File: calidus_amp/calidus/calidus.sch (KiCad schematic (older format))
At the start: 15 parts, among them J1 power, J10 led_overload, J11 led_power, J2 input, J3 prevs, J4 icsp, J5 service, J6 sense_bus, J7 left_out, J8 right_out, J9 mute_key

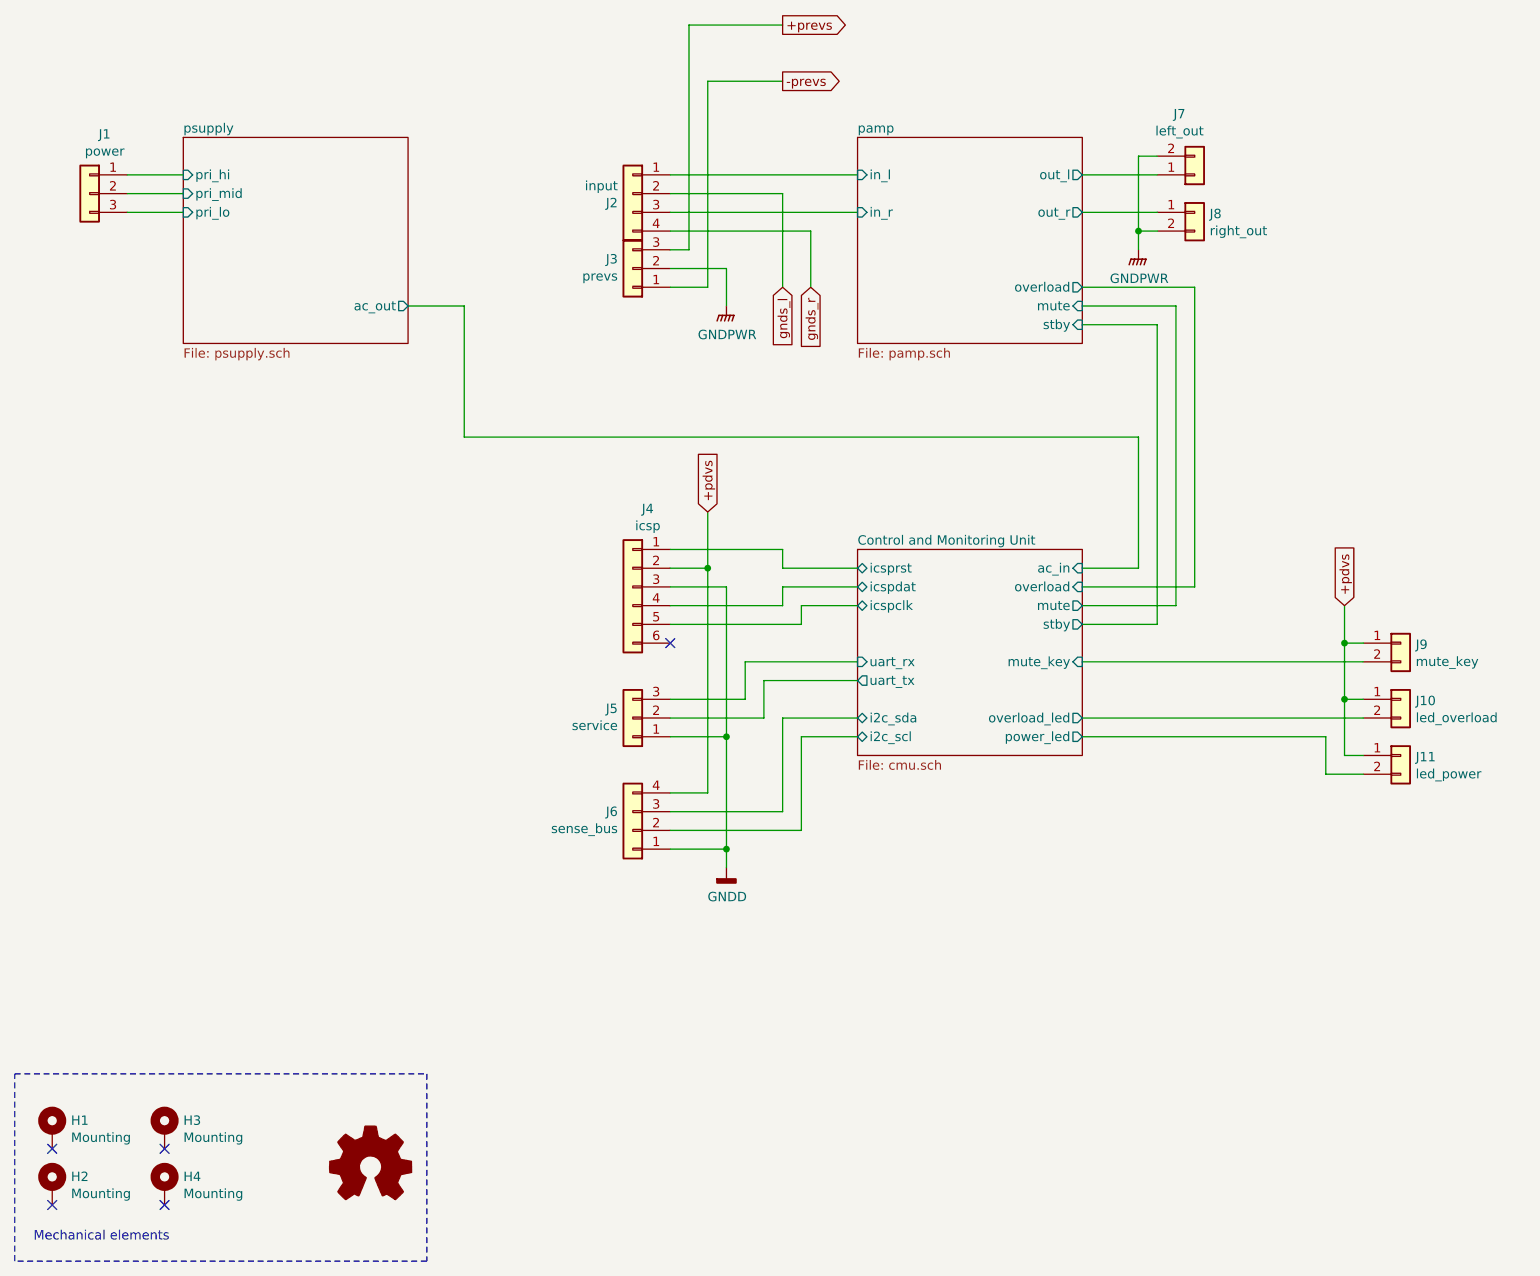
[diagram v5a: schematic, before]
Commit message: WIP: Component placement on PCB
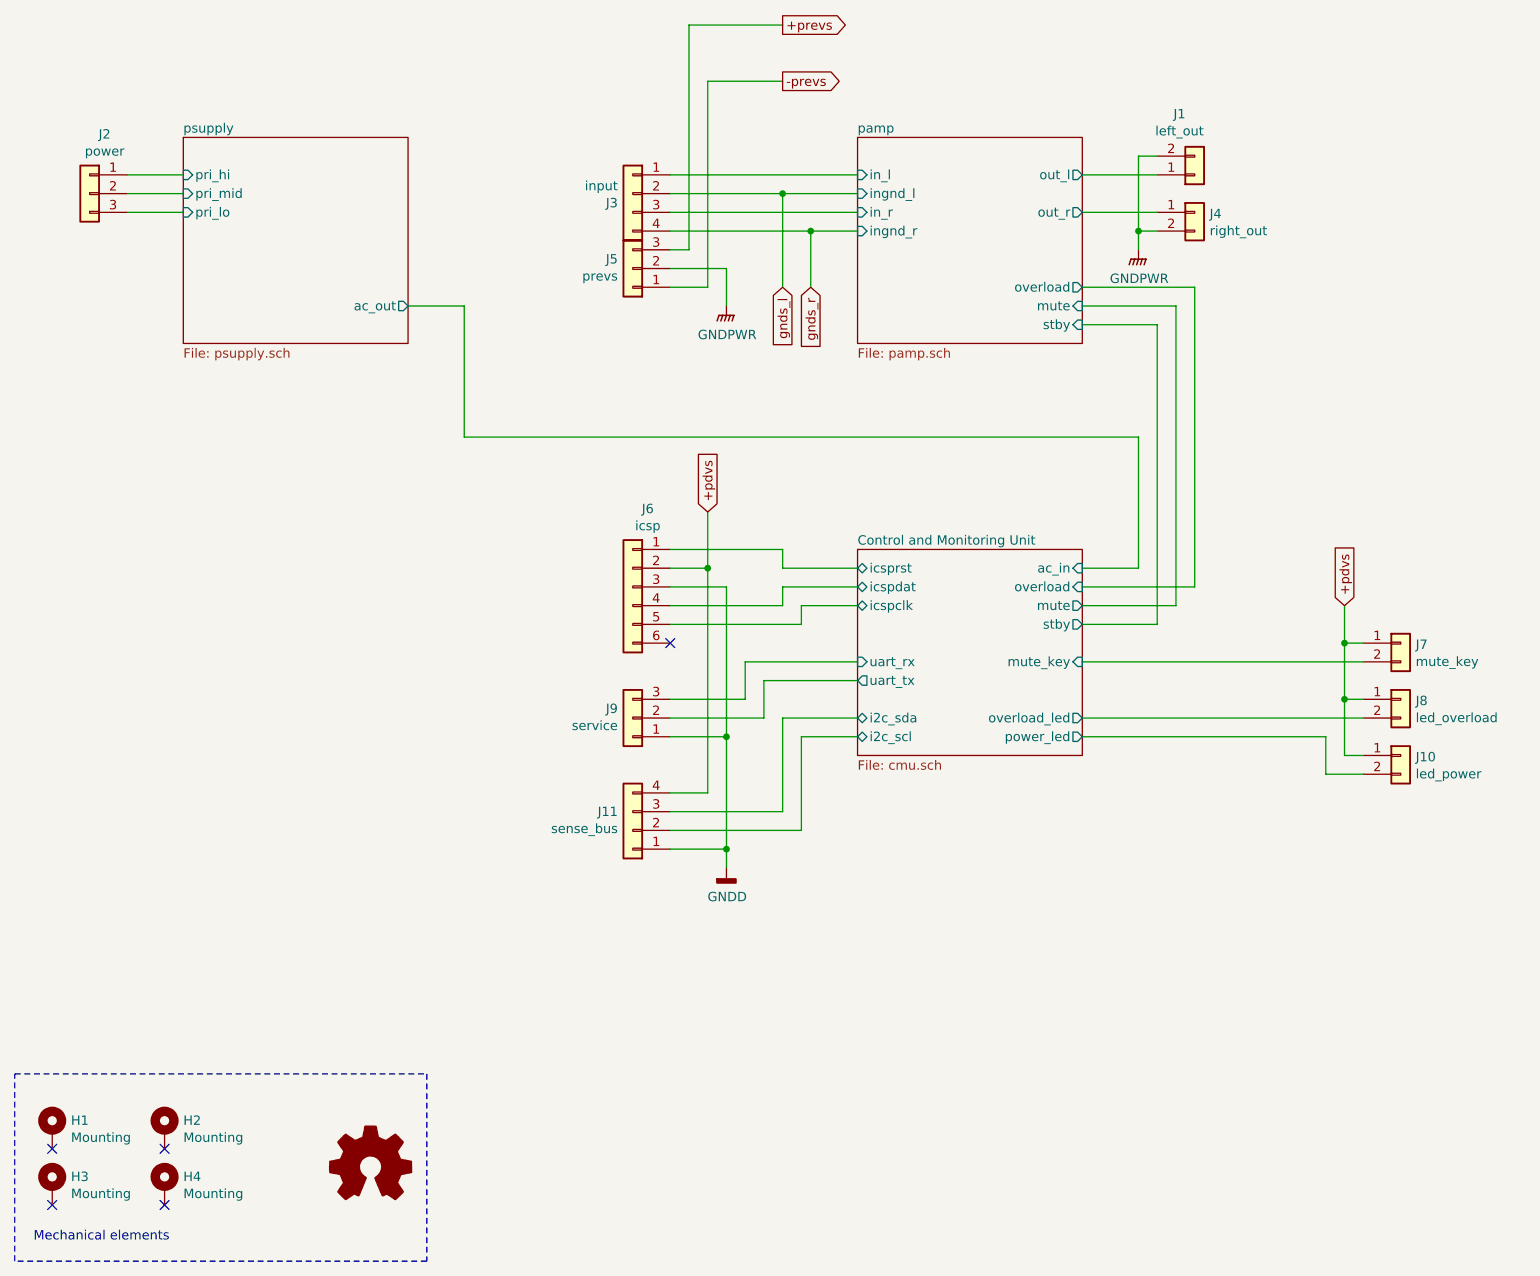
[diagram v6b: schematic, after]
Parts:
- renumbered H3 to H2, H2 to H3, J7 to J1, J11 to J10, J6 to J11, J1 to J2, J2 to J3, J8 to J4, J3 to J5, J4 to J6, J9 to J7, J10 to J8, J5 to J9
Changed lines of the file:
@@
 F7 "out_r" O R 6700 2000 50
 F8 "stby" I R 6700 2600 50
+F9 "ingnd_l" I L 5500 1900 50
+F10 "ingnd_r" I L 5500 2100 50
 $EndSheet
 $Comp
-L Connector_Generic:Conn_01x03 J1
+L Connector_Generic:Conn_01x03 J2
 U 1 1 5C47FAB8
 P 1400 1900
-F 0 "J1" H 1320 2217 50  0000 C CNN
+F 0 "J2" H 1320 2217 50  0000 C CNN
 F 1 "power" H 1320 2126 50  0000 C CNN
 F 2 "Connector_Phoenix_MC:PhoenixContact_MCV_1,5_3-G-3.5_1x03_P3.50mm_Vertical" H 1400 1900 50  0001 C CNN
@@
 	5100 1900 4500 1900
 $Comp
-L Connector_Generic:Conn_01x02 J7
+L Connector_Generic:Conn_01x02 J1
 U 1 1 5C47FBF8
 P 7300 1800
-F 0 "J7" H 7219 1475 50  0000 C CNN
+F 0 "J1" H 7219 1475 50  0000 C CNN
 F 1 "left_out" H 7219 1566 50  0000 C CNN
 F 2 "Connector_Phoenix_MC:PhoenixContact_MCV_1,5_2-G-3.5_1x02_P3.50mm_Vertical" H 7300 1800 50  0001 C CNN
@@
 $EndComp
 $Comp
-L Connector_Generic:Conn_01x02 J8
+L Connector_Generic:Conn_01x02 J4
 U 1 1 5C47FC30
 P 7300 2000
-F 0 "J8" H 7380 1992 50  0000 L CNN
+F 0 "J4" H 7380 1992 50  0000 L CNN
 F 1 "right_out" H 7380 1901 50  0000 L CNN
 F 2 "Connector_Phoenix_MC:PhoenixContact_MCV_1,5_2-G-3.5_1x02_P3.50mm_Vertical" H 7300 2000 50  0001 C CNN
@@
 	7000 2100 7100 2100
 $Comp
-L power:GNDPWR #PWR04
+L power:GNDPWR #PWR01
 U 1 1 5C47FEE1
 P 7000 2200
-F 0 "#PWR04" H 7000 2000 50  0001 C CNN
+F 0 "#PWR01" H 7000 2000 50  0001 C CNN
 F 1 "GNDPWR" H 7004 2046 50  0000 C CNN
 F 2 "" H 7000 2150 50  0001 C CNN
@@
 +pdvs
 $Comp
-L Connector_Generic:Conn_01x02 J10
+L Connector_Generic:Conn_01x02 J8
 U 1 1 5C4DAFE8
 P 8400 4600
-F 0 "J10" H 8480 4592 50  0000 L CNN
+F 0 "J8" H 8480 4592 50  0000 L CNN
 F 1 "led_overload" H 8480 4501 50  0000 L CNN
 F 2 "Connector_PinHeader_2.54mm:PinHeader_1x02_P2.54mm_Vertical" H 8400 4600 50  0001 C CNN
@@
 $EndComp
 $Comp
-L Connector_Generic:Conn_01x02 J11
+L Connector_Generic:Conn_01x02 J10
 U 1 1 5C4DB050
 P 8400 4900
-F 0 "J11" H 8480 4892 50  0000 L CNN
+F 0 "J10" H 8480 4892 50  0000 L CNN
 F 1 "led_power" H 8480 4801 50  0000 L CNN
 F 2 "Connector_PinHeader_2.54mm:PinHeader_1x02_P2.54mm_Vertical" H 8400 4900 50  0001 C CNN
@@
 Connection ~ 8100 4600
 $Comp
-L Connector_Generic:Conn_01x02 J9
+L Connector_Generic:Conn_01x02 J7
 U 1 1 5C4E1437
 P 8400 4300
-F 0 "J9" H 8480 4292 50  0000 L CNN
+F 0 "J7" H 8480 4292 50  0000 L CNN
 F 1 "mute_key" H 8480 4201 50  0000 L CNN
 F 2 "Connector_PinHeader_2.54mm:PinHeader_1x02_P2.54mm_Vertical" H 8400 4300 50  0001 C CNN
@@
 	7000 3900 6700 3900
 $Comp
-L Connector_Generic:Conn_01x06 J4
+L Connector_Generic:Conn_01x06 J6
 U 1 1 5C4F09AA
 P 4300 4000
-F 0 "J4" H 4220 4417 50  0000 C CNN
+F 0 "J6" H 4220 4417 50  0000 C CNN
 F 1 "icsp" H 4220 4326 50  0000 C CNN
 F 2 "Connector_PinHeader_2.54mm:PinHeader_1x06_P2.54mm_Vertical" H 4300 4000 50  0001 C CNN
@@
 P 4800 5500
 AR Path="/5C43C4AB/5C504FC8" Ref="#PWR?"  Part="1"
-AR Path="/5C504FC8" Ref="#PWR02"  Part="1"
-F 0 "#PWR02" H 4800 5250 50  0001 C CNN
+AR Path="/5C504FC8" Ref="#PWR03"  Part="1"
+F 0 "#PWR03" H 4800 5250 50  0001 C CNN
 F 1 "GNDD" H 4804 5345 50  0000 C CNN
 F 2 "" H 4800 5500 50  0001 C CNN
@@
 	4500 4200 5200 4200
 $Comp
-L Connector_Generic:Conn_01x03 J5
+L Connector_Generic:Conn_01x03 J9
 U 1 1 5C51607F
 P 4300 4700
-F 0 "J5" H 4380 4650 50  0000 L CNN
+F 0 "J9" H 4380 4650 50  0000 L CNN
 F 1 "service" H 4380 4741 50  0000 L CNN
 F 2 "Connector_PinHeader_2.54mm:PinHeader_1x03_P2.54mm_Vertical" H 4300 4700 50  0001 C CNN
@@
 	4800 4000 4500 4000
 $Comp
-L Connector_Generic:Conn_01x04 J6
+L Connector_Generic:Conn_01x04 J11
 U 1 1 5C5CE216
 P 4300 5300
-F 0 "J6" H 4380 5200 50  0000 L CNN
+F 0 "J11" H 4380 5200 50  0000 L CNN
 F 1 "sense_bus" H 4380 5291 50  0000 L CNN
 F 2 "Connector_PinHeader_2.54mm:PinHeader_1x04_P2.54mm_Vertical" H 4300 5300 50  0001 C CNN
@@
 NoConn ~ 1200 7000
 $Comp
-L Mechanical:MountingHole_Pad H2
+L Mechanical:MountingHole_Pad H3
 U 1 1 5C581F06
 P 1200 7200
-F 0 "H2" H 1300 7251 50  0000 L CNN
+F 0 "H3" H 1300 7251 50  0000 L CNN
 F 1 "Mounting" H 1300 7160 50  0000 L CNN
 F 2 "MountingHole:MountingHole_3.2mm_M3_Pad" H 1200 7200 50  0001 C CNN
@@
 NoConn ~ 1200 7300
 $Comp
-L Mechanical:MountingHole_Pad H3
+L Mechanical:MountingHole_Pad H2
 U 1 1 5C5841CE
 P 1800 6900
-F 0 "H3" H 1900 6951 50  0000 L CNN
+F 0 "H2" H 1900 6951 50  0000 L CNN
 F 1 "Mounting" H 1900 6860 50  0000 L CNN
 F 2 "MountingHole:MountingHole_3.2mm_M3_Pad" H 1800 6900 50  0001 C CNN
@@
 Mechanical elements
 $Comp
-L power:GNDPWR #PWR01
+L power:GNDPWR #PWR02
 U 1 1 5C50E81E
 P 4800 2500
-F 0 "#PWR01" H 4800 2300 50  0001 C CNN
+F 0 "#PWR02" H 4800 2300 50  0001 C CNN
 F 1 "GNDPWR" H 4804 2346 50  0000 C CNN
 F 2 "" H 4800 2450 50  0001 C CNN
@@
 	4600 1000 5100 1000
 $Comp
-L Connector_Generic:Conn_01x04 J2
+L Connector_Generic:Conn_01x04 J3
 U 1 1 5C540E50
 P 4300 1900
-F 0 "J2" H 4380 1850 50  0000 L CNN
+F 0 "J3" H 4380 1850 50  0000 L CNN
 F 1 "input" H 4380 1941 50  0000 L CNN
 F 2 "Connector_Phoenix_MC:PhoenixContact_MCV_1,5_3-G-3.5_1x03_P3.50mm_Vertical" H 4300 1900 50  0001 C CNN
@@
 $EndComp
 $Comp
-L Connector_Generic:Conn_01x03 J3
+L Connector_Generic:Conn_01x03 J5
 U 1 1 5C540ED0
 P 4300 2300
-F 0 "J3" H 4380 2250 50  0000 L CNN
+F 0 "J5" H 4380 2250 50  0000 L CNN
 F 1 "prevs" H 4380 2341 50  0000 L CNN
 F 2 "Connector_Phoenix_MC:PhoenixContact_MCV_1,5_3-G-3.5_1x03_P3.50mm_Vertical" H 4300 2300 50  0001 C CNN
@@
 Wire Wire Line
 	5250 2100 4500 2100
+Wire Wire Line
+	5500 1900 5100 1900
+Connection ~ 5100 1900
+Wire Wire Line
+	5500 2100 5250 2100
+Connection ~ 5250 2100
 $EndSCHEMATC

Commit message: WIP: Component placement and footpring assignment
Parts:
- J1, J4: footprint Connector_Phoenix_MC:PhoenixContact_MCV_1,5_2-G-3.5_1x02_P3.50mm_Vertical -> Connector_Phoenix_MC:PhoenixContact_MCV_1,5_2-G-3.81_1x02_P3.81mm_Vertical
- J2: footprint Connector_Phoenix_MC:PhoenixContact_MCV_1,5_3-G-3.5_1x03_P3.50mm_Vertical -> Connector_Phoenix_MC:PhoenixContact_MCV_1,5_3-G-3.81_1x03_P3.81mm_Vertical
- J3: footprint Connector_Phoenix_MC:PhoenixContact_MCV_1,5_3-G-3.5_1x03_P3.50mm_Vertical -> Connector_Phoenix_MC:PhoenixContact_MCV_1,5_4-G-3.5_1x04_P3.50mm_Vertical
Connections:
- net gnds_l: now also J3.3 (Pin_3); no longer J3.2 (Pin_2)
- net gnds_r: now also J3.1 (Pin_1); no longer J3.4 (Pin_4)
- net pamp/in_l: now also J3.4 (Pin_4); no longer J3.1 (Pin_1)
- net pamp/in_r: now also J3.2 (Pin_2); no longer J3.3 (Pin_3)
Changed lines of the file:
@@
 F 0 "J2" H 1320 2217 50  0000 C CNN
 F 1 "power" H 1320 2126 50  0000 C CNN
-F 2 "Connector_Phoenix_MC:PhoenixContact_MCV_1,5_3-G-3.5_1x03_P3.50mm_Vertical" H 1400 1900 50  0001 C CNN
+F 2 "Connector_Phoenix_MC:PhoenixContact_MCV_1,5_3-G-3.81_1x03_P3.81mm_Vertical" H 1400 1900 50  0001 C CNN
 F 3 "~" H 1400 1900 50  0001 C CNN
 	1    1400 1900
@@
 F 0 "J1" H 7219 1475 50  0000 C CNN
 F 1 "left_out" H 7219 1566 50  0000 C CNN
-F 2 "Connector_Phoenix_MC:PhoenixContact_MCV_1,5_2-G-3.5_1x02_P3.50mm_Vertical" H 7300 1800 50  0001 C CNN
+F 2 "Connector_Phoenix_MC:PhoenixContact_MCV_1,5_2-G-3.81_1x02_P3.81mm_Vertical" H 7300 1800 50  0001 C CNN
 F 3 "~" H 7300 1800 50  0001 C CNN
 	1    7300 1800
@@
 F 0 "J4" H 7380 1992 50  0000 L CNN
 F 1 "right_out" H 7380 1901 50  0000 L CNN
-F 2 "Connector_Phoenix_MC:PhoenixContact_MCV_1,5_2-G-3.5_1x02_P3.50mm_Vertical" H 7300 2000 50  0001 C CNN
+F 2 "Connector_Phoenix_MC:PhoenixContact_MCV_1,5_2-G-3.81_1x02_P3.81mm_Vertical" H 7300 2000 50  0001 C CNN
 F 3 "~" H 7300 2000 50  0001 C CNN
 	1    7300 2000
@@
 L Connector_Generic:Conn_01x04 J3
 U 1 1 5C540E50
-P 4300 1900
-F 0 "J3" H 4380 1850 50  0000 L CNN
-F 1 "input" H 4380 1941 50  0000 L CNN
-F 2 "Connector_Phoenix_MC:PhoenixContact_MCV_1,5_3-G-3.5_1x03_P3.50mm_Vertical" H 4300 1900 50  0001 C CNN
-F 3 "~" H 4300 1900 50  0001 C CNN
-	1    4300 1900
-	-1   0    0    -1
-$EndComp
-$Comp
+P 4300 2000
+F 0 "J3" H 4220 1575 50  0000 C CNN
+F 1 "input" H 4220 1666 50  0000 C CNN
+F 2 "Connector_Phoenix_MC:PhoenixContact_MCV_1,5_4-G-3.5_1x04_P3.50mm_Vertical" H 4300 2000 50  0001 C CNN
+F 3 "~" H 4300 2000 50  0001 C CNN
+	1    4300 2000
+	-1   0    0    1
+$EndComp
+$Comp
